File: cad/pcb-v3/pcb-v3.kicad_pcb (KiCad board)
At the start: 4 copper layers, 19.3 x 19.3 mm, 46 parts

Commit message: pcb-v3: C1/C2 0603->0402 into the packer, C5/C7 0805->0603, left column down to U3+U4. 22 parts in 22 slots. Route: 12 -> 7 opens, plane untouched naturally, min track 0.200, vias 0.6/0.3.
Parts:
- moved C6 17.6 mm to (-2.90, -7.90)
- moved ROV2 13.0 mm to (6.15, 5.06)
- moved C1 9.44 mm to (-0.70, -7.90), turned to 90 degrees
- moved C2 5.62 mm to (-5.10, -7.90), turned to 90 degrees
- moved C12 5.52 mm to (-8.50, -2.50)
- moved R5 5.52 mm to (-7.35, -2.50)
- moved R3 5.50 mm to (3.70, -7.90)
- moved R1 3.30 mm to (2.60, -7.90)
- moved C10 2.25 mm to (-6.25, -7.90)
- moved C13 2.25 mm to (-8.50, -7.90)
- moved R4 2.25 mm to (-7.35, -7.90)
- moved R2 2.25 mm to (4.85, -7.90)
- moved R6 2.20 mm to (1.50, -7.90)
- moved R7 2.20 mm to (-1.80, -7.90)
- moved ROK3 2.19 mm to (6.15, 7.25)
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
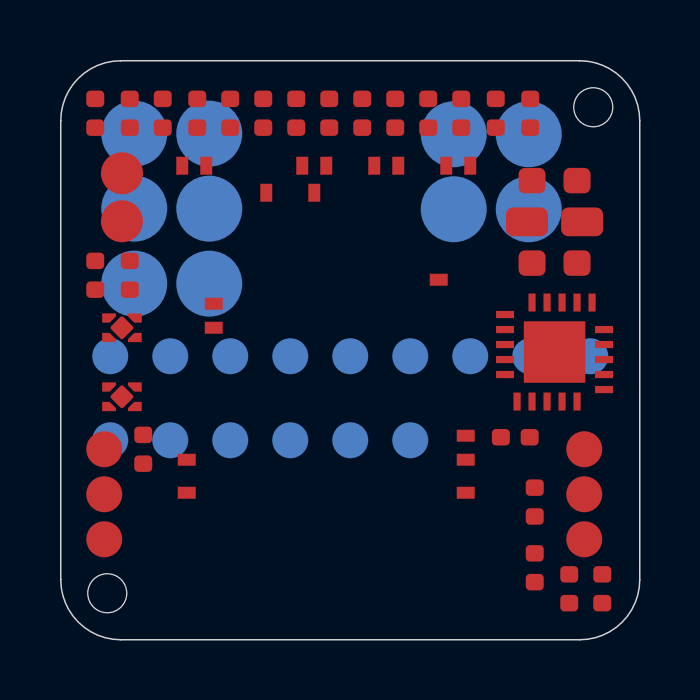
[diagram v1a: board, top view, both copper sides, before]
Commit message: pcb-v3: silkscreen (F.Fab designators, pin-1 dots, back identity block). Fix two checker bugs: KiCad Y-down rotation sign (79 phantom shorts) and rule-area layer scoping (47 phantom boxed pads). All gates clean; 7 opens, plane intact.
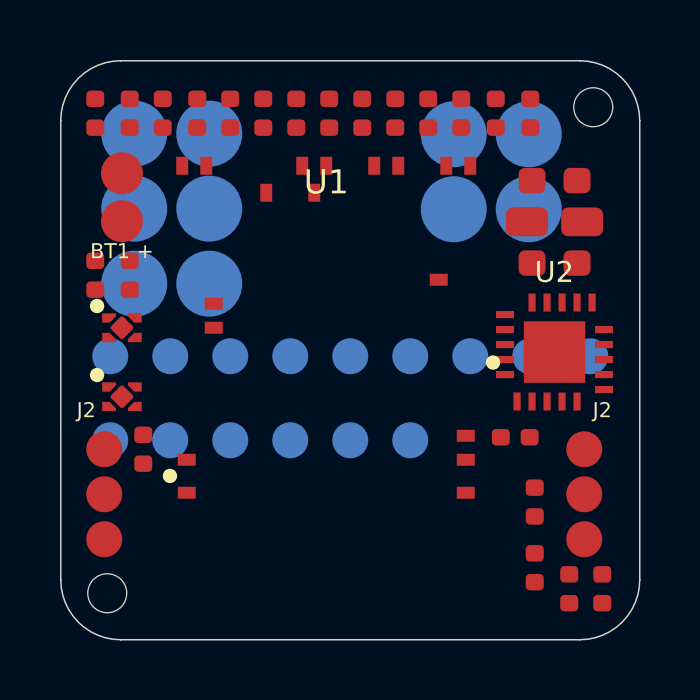
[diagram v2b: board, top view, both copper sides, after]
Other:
- board text added: "BT1 +"
- board text added: "Daniel Rivera"
- board text added: "J2"
- board text added: "TouchID v3 2026"
- board text added: "U1"
- board text added: "U2"
- board text added: "driver0"

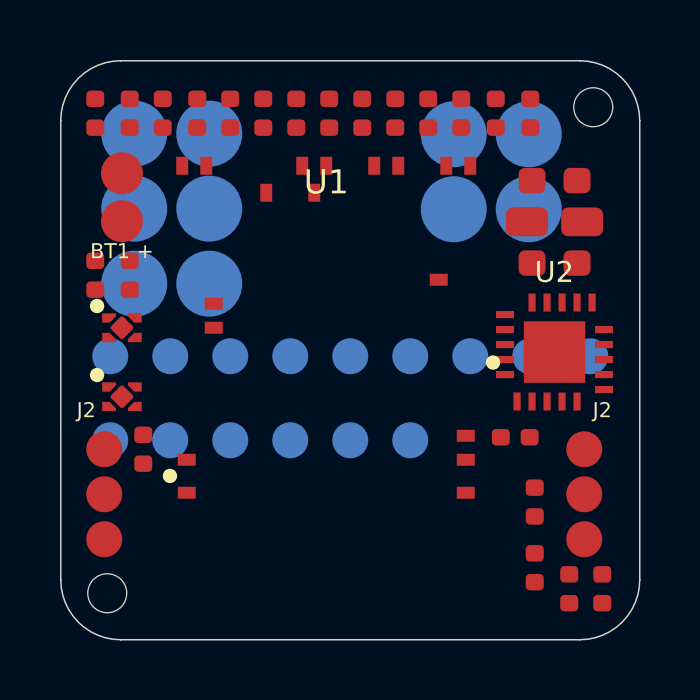
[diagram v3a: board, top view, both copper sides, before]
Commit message: pcb-v3: re-source footprints from JLCPCB (L1 0.96->2.20mm was badly wrong), keep TI's land for U2 where JLC's is wider and riskier. Remove name from silk, add connector pinout labels + pin-1 dots.
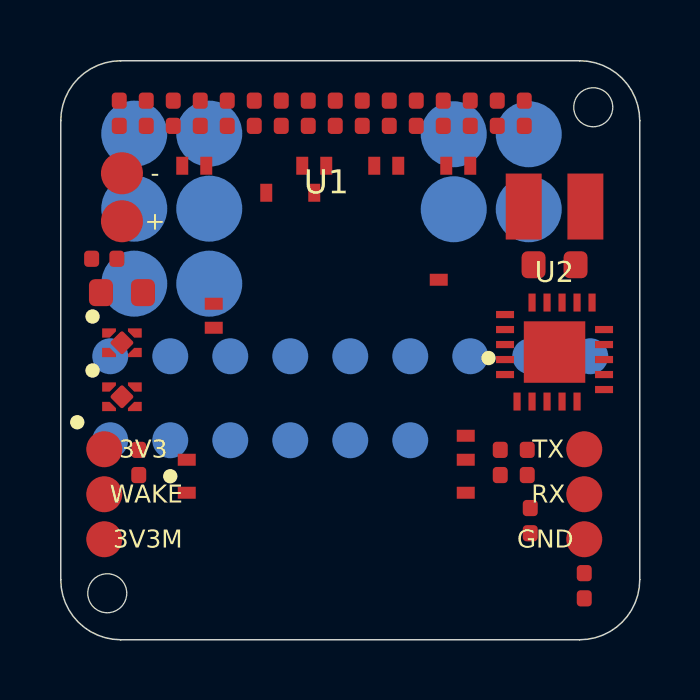
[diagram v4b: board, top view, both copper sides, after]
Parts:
- moved C5 14.9 mm to (-7.61, -1.92)
- moved ROV2 13.0 mm to (5.80, -7.90)
- moved R5 5.41 mm to (-7.70, -7.90)
- moved ROK3 3.52 mm to (5.90, 3.74)
- moved ROK2 2.62 mm to (6.00, 5.68)
- moved C2 1.90 mm to (-3.20, -7.90)
- moved C13 1.70 mm to (-6.80, -7.90)
- moved R6 1.60 mm to (3.10, -7.90)
- moved R3 1.50 mm to (2.20, -7.90)
- moved R4 1.45 mm to (-5.90, -7.90)
- moved R1 1.30 mm to (1.30, -7.90)
- moved C10 1.25 mm to (-5.00, -7.90)
- moved ROV1 1.10 mm to (4.90, -7.90)
- moved C4 0.98 mm to (5.00, 3.74), turned to 90 degrees
- moved R2 0.85 mm to (4.00, -7.90)
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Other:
- board text added: "+"
- board text added: "-"
- board text added: "3V3"
- board text added: "3V3M"
- board text added: "CLK"
- board text added: "DIO"
- board text added: "GND"
- board text added: "RST"
- board text added: "RX"
- board text added: "TX"
- board text added: "VDD"
- board text added: "WAKE"
- board text removed: "BT1 +"
- board text removed: "Daniel Rivera"
- board text removed: "J2"

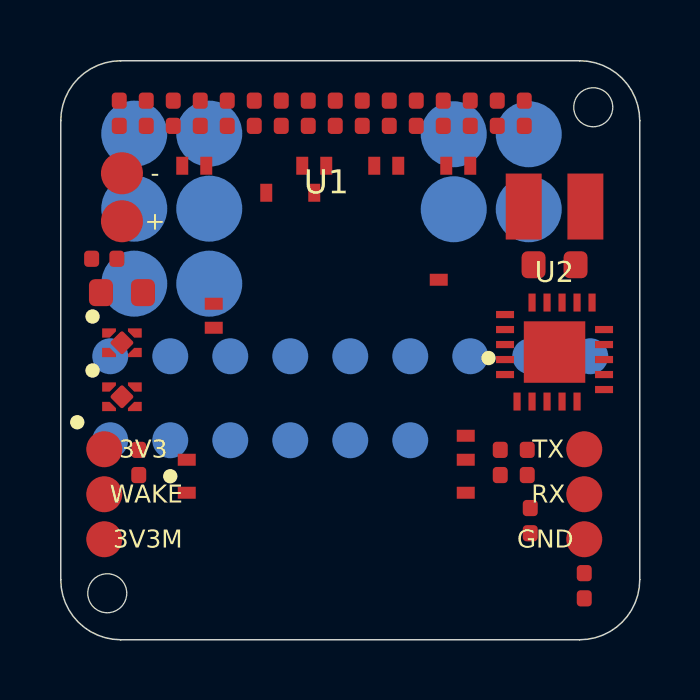
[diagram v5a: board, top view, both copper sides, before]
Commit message: preflight.py: single pre-order gate (15 checks). Found 3 checker bugs of my own (pad-net regex scope, layer-blind keep-outs, silk-vs-wrong-side pads) and 2 real issues (silk over pads, LX has no 0.40 trunk). 13/15 pass.
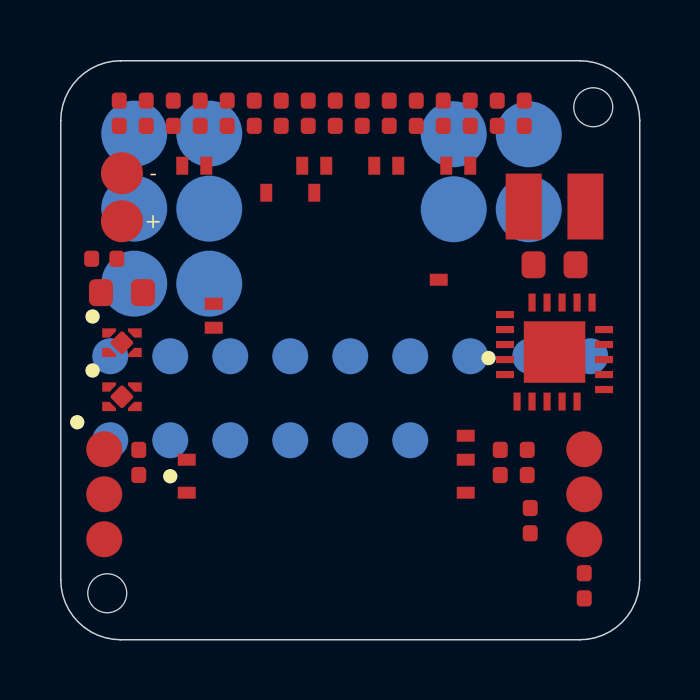
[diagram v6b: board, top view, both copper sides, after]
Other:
- board text removed: "U1"
- board text removed: "U2"
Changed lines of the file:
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@@
-	)
-	(gr_text
-		"U1"
-		(at -0.8 -5.6)
-		(layer "F.SilkS")
-		(effects (font (size 0.8 0.8) (thickness 0.1)))
-	)
-	(gr_text
-		"U2"
-		(at 6.8 -2.6)
-		(layer "F.SilkS")
-		(effects (font (size 0.7 0.7) (thickness 0.1)))
 	)
 	(gr_text
 		"3V3"
-		(at -6.9 3.3)
-		(layer "F.SilkS")
-		(effects (font (size 0.6 0.6) (thickness 0.1)))
-	)
-	(gr_text
-		"3V3"
-		(at -6.9 3.3)
+		(at -6.888 3.3)
 		(layer "F.Fab")
 		(effects (font (size 0.4 0.4) (thickness 0.06)))
@@
 	(gr_text
 		"WAKE"
-		(at -6.8 4.8)
-		(layer "F.SilkS")
-		(effects (font (size 0.6 0.6) (thickness 0.1)))
-	)
-	(gr_text
-		"WAKE"
-		(at -6.8 4.8)
+		(at -6.7 4.8)
 		(layer "F.Fab")
 		(effects (font (size 0.4 0.4) (thickness 0.06)))
@@
 	(gr_text
 		"3V3M"
-		(at -6.75 6.3)
-		(layer "F.SilkS")
-		(effects (font (size 0.6 0.6) (thickness 0.1)))
-	)
-	(gr_text
-		"3V3M"
-		(at -6.75 6.3)
+		(at -6.7 6.3)
 		(layer "F.Fab")
 		(effects (font (size 0.4 0.4) (thickness 0.06)))
@@
 	(gr_text
 		"TX"
-		(at 6.6 3.3)
-		(layer "F.SilkS")
-		(effects (font (size 0.6 0.6) (thickness 0.1)))
-	)
-	(gr_text
-		"TX"
-		(at 6.6 3.3)
+		(at 6.675 3.3)
 		(layer "F.Fab")
 		(effects (font (size 0.4 0.4) (thickness 0.06)))
@@
 	(gr_text
 		"RX"
-		(at 6.6 4.8)
-		(layer "F.SilkS")
-		(effects (font (size 0.6 0.6) (thickness 0.1)))
-	)
-	(gr_text
-		"RX"
-		(at 6.6 4.8)
+		(at 6.675 4.8)
 		(layer "F.Fab")
 		(effects (font (size 0.4 0.4) (thickness 0.06)))
@@
 	(gr_text
 		"GND"
-		(at 6.5 6.3)
-		(layer "F.SilkS")
-		(effects (font (size 0.6 0.6) (thickness 0.1)))
-	)
-	(gr_text
-		"GND"
-		(at 6.5 6.3)
+		(at 6.488 6.3)
 		(layer "F.Fab")
 		(effects (font (size 0.4 0.4) (thickness 0.06)))
@@
 	(gr_text
 		"DIO"
-		(at -8.0 1.9)
-		(layer "B.SilkS")
-		(effects (font (size 0.6 0.6) (thickness 0.1)) (justify mirror))
-	)
-	(gr_text
-		"DIO"
-		(at -8.0 1.9)
+		(at -8.0 2.0)
 		(layer "F.Fab")
 		(effects (font (size 0.4 0.4) (thickness 0.06)))
@@
 	(gr_text
 		"CLK"
-		(at -6.0 1.9)
-		(layer "B.SilkS")
-		(effects (font (size 0.6 0.6) (thickness 0.1)) (justify mirror))
-	)
-	(gr_text
-		"CLK"
-		(at -6.0 1.9)
+		(at -6.0 2.0)
 		(layer "F.Fab")
 		(effects (font (size 0.4 0.4) (thickness 0.06)))
@@
 	(gr_text
 		"RST"
-		(at -4.0 1.9)
-		(layer "B.SilkS")
-		(effects (font (size 0.6 0.6) (thickness 0.1)) (justify mirror))
-	)
-	(gr_text
-		"RST"
-		(at -4.0 1.9)
+		(at -4.0 2.0)
 		(layer "F.Fab")
 		(effects (font (size 0.4 0.4) (thickness 0.06)))
@@
 	(gr_text
 		"VDD"
-		(at -2.0 1.9)
-		(layer "B.SilkS")
-		(effects (font (size 0.6 0.6) (thickness 0.1)) (justify mirror))
-	)
-	(gr_text
-		"VDD"
-		(at -2.0 1.9)
+		(at -2.0 2.0)
 		(layer "F.Fab")
 		(effects (font (size 0.4 0.4) (thickness 0.06)))
@@
 	(gr_text
 		"GND"
-		(at 0.0 1.9)
-		(layer "B.SilkS")
-		(effects (font (size 0.6 0.6) (thickness 0.1)) (justify mirror))
-	)
-	(gr_text
-		"GND"
-		(at 0.0 1.9)
+		(at 0.0 2.0)
 		(layer "F.Fab")
 		(effects (font (size 0.4 0.4) (thickness 0.06)))
@@
 	(gr_text
 		"+"
-		(at -6.51 -4.3)
+		(at -6.572 -4.3)
 		(layer "F.SilkS")
-		(effects (font (size 0.6 0.6) (thickness 0.1)))
+		(effects (font (size 0.5 0.5) (thickness 0.1)))
 	)
 	(gr_text
 		"+"
-		(at -6.51 -4.3)
+		(at -6.572 -4.3)
 		(layer "F.Fab")
 		(effects (font (size 0.4 0.4) (thickness 0.06)))
@@
 	(gr_text
 		"-"
-		(at -6.51 -5.9)
+		(at -6.572 -5.9)
 		(layer "F.SilkS")
-		(effects (font (size 0.6 0.6) (thickness 0.1)))
+		(effects (font (size 0.5 0.5) (thickness 0.1)))
 	)
 	(gr_text
 		"-"
-		(at -6.51 -5.9)
+		(at -6.572 -5.9)
 		(layer "F.Fab")
 		(effects (font (size 0.4 0.4) (thickness 0.06)))

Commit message: U2 land was 0.25mm off its own centreline (even-count offset formula for an odd pad row). LX wrapped 11mm around the chip; L1 moved above U2 and flipped -> 1.91mm. Opens 8->7.
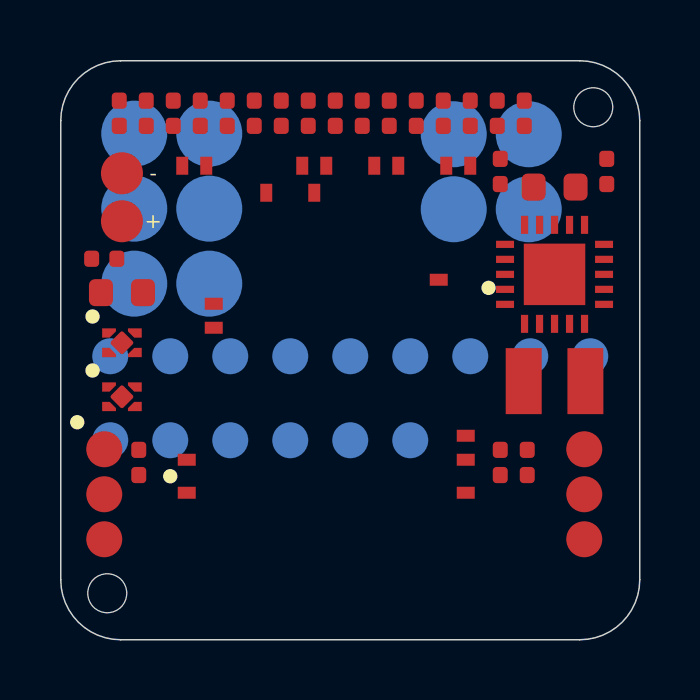
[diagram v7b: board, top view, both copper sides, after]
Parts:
- moved ROK1 15.9 mm to (5.80, -7.90)
- moved C1 12.9 mm to (5.00, 3.74)
- moved R3 12.2 mm to (5.90, 3.74)
- moved ROK2 11.9 mm to (8.55, -5.96)
- moved C4 11.8 mm to (3.10, -7.90)
- moved ROK3 11.7 mm to (4.90, -7.90)
- moved L1 5.82 mm to (6.81, 1.03), turned to 180 degrees
- moved R6 3.60 mm to (-0.50, -7.90)
- moved C7 2.59 mm to (6.81, -5.44)
- moved U2 2.59 mm to (6.81, -2.53)
- moved ROV1 1.94 mm to (5.00, -5.96)
- moved R2 1.80 mm to (2.20, -7.90)
- moved ROV2 1.80 mm to (4.00, -7.90)

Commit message: C7 out of the right column so U2 gets a via lane: opens 7->5, boxed-in pads 3->1. 12/15 preflight checks pass.
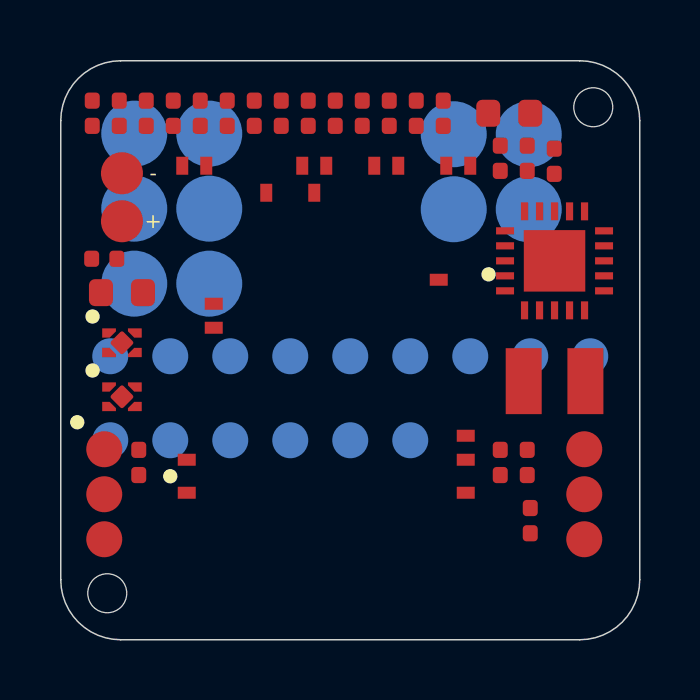
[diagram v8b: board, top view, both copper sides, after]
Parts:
- moved ROK1 11.6 mm to (5.90, 3.74)
- moved C7 2.89 mm to (5.30, -7.90)
- moved ROV1 2.72 mm to (3.10, -7.90)
- moved C1 2.18 mm to (6.00, 5.68)
- moved ROK3 1.80 mm to (5.90, -6.40)
- moved ROV2 1.80 mm to (5.00, -6.40)
- moved R1 1.80 mm to (-0.50, -7.90)
- moved ROK2 1.78 mm to (6.80, -6.30)
- moved C10 0.90 mm to (-5.90, -7.90)
- moved C13 0.90 mm to (-7.70, -7.90)
- moved C3 0.90 mm to (-5.00, -7.90)
- moved C6 0.90 mm to (-3.20, -7.90)
- moved R3 0.90 mm to (5.00, 3.74)
- moved R2 0.90 mm to (1.30, -7.90)
- moved C4 0.90 mm to (2.20, -7.90)
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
